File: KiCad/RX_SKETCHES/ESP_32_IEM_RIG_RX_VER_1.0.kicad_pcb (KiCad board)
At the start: 2 copper layers, 55.2 x 90.5 mm, 69 parts, among them J1 AudioJack3, J6 USB_C_Receptacle_USB2.0_16P, Q1 S8050, Q2 S8050, SW2 FILTER_MODE, SW3 SOFT_MUTE, SW4 ON/OFF, U1 PCM5102, U2 ESP32-WROOM-32U, U3 MAX97220AETE_T, U4 LM3940IMPX-3.3_NOPB, U5 CP2102C-Axx-xQFN24

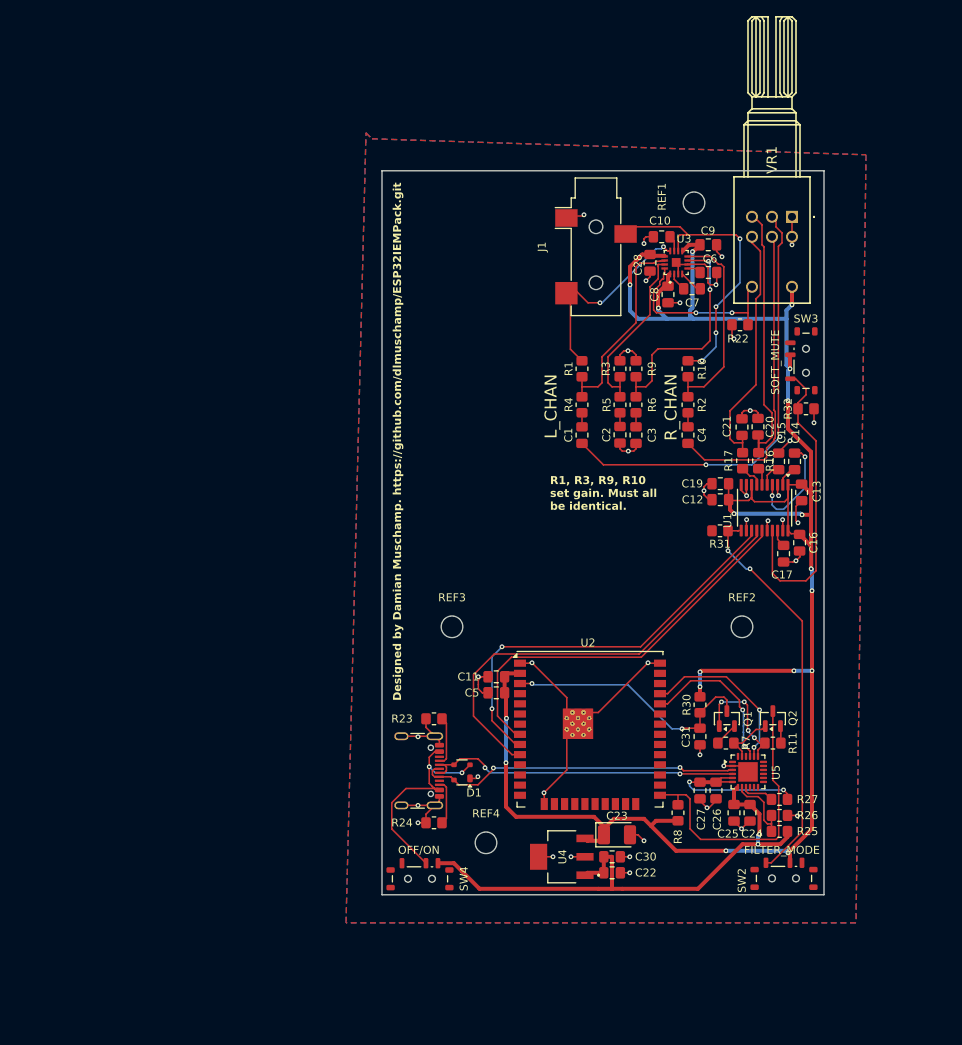
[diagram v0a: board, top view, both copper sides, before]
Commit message: Ship RX+TX v1 boards: routed PCBs, JLCPCB exports, README for order spin.
Freeze electrical intent for fab (Gerbers/BOM/CPL), document firmware design philosophy and summer timeline, and drop stale ERC/DRC/fab clutter.

Co-authored-by: Cursor <cursoragent@cursor.com>
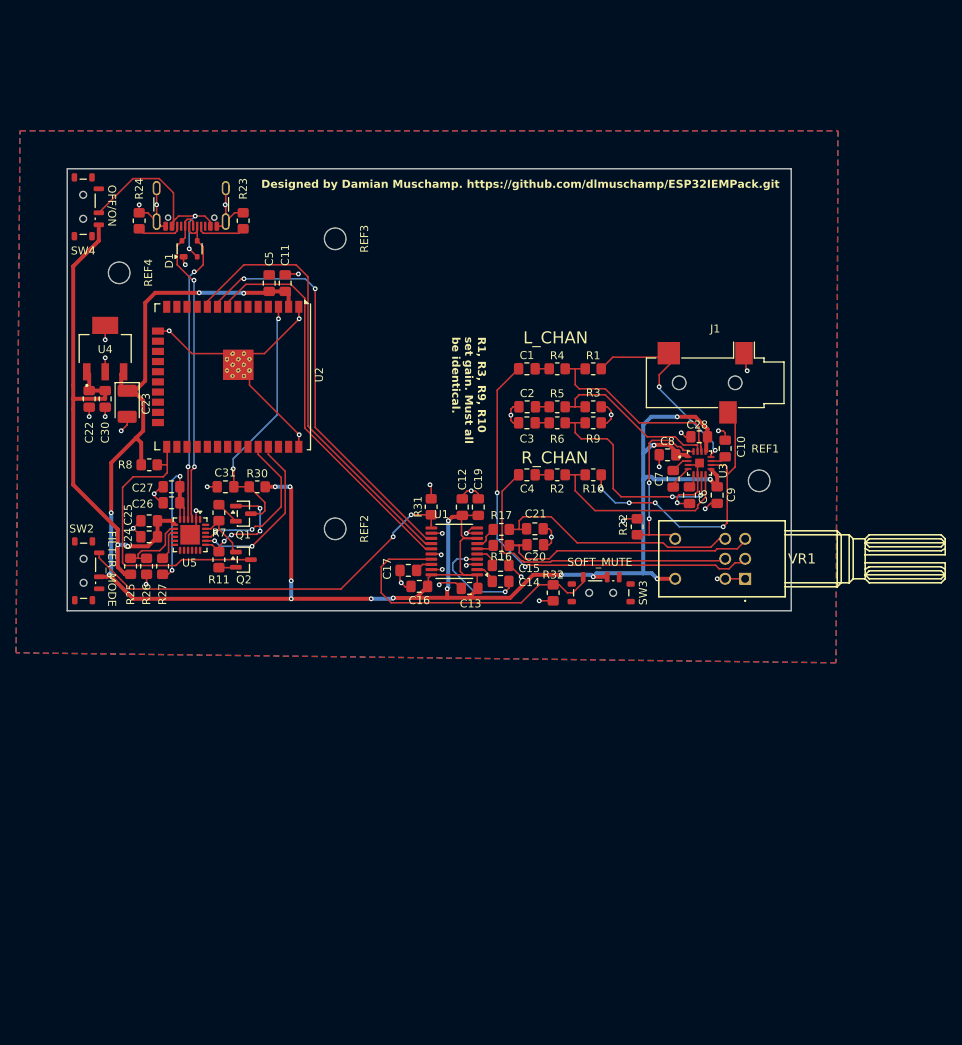
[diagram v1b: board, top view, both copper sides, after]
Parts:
- moved SW2 95.6 mm to (59.2, 88.5), turned to -90 degrees
- moved SW4 94.0 mm to (59.1, 43.0), turned to -90 degrees
- moved C22 88.2 mm to (59.9, 67.0), turned to -90 degrees
- moved R25 87.6 mm to (65.1, 87.9), turned to 90 degrees
- moved U4 85.4 mm to (61.9, 60.7), turned to 90 degrees
- moved C30 85.4 mm to (61.9, 67.0), turned to -90 degrees
- moved R26 85.0 mm to (67.1, 87.9), turned to -90 degrees
- moved REF4 84.7 mm to (63.6, 51.2), turned to -90 degrees
- moved R24 83.8 mm to (66.2, 44.8), turned to 90 degrees
- moved C24 82.6 mm to (67.4, 84.2), turned to 180 degrees
- moved R27 82.4 mm to (69.1, 87.9), turned to -90 degrees
- moved C25 81.7 mm to (67.4, 82.2), turned to 180 degrees
- moved C23 81.6 mm to (64.7, 67.6), turned to -90 degrees
- moved R8 79.1 mm to (67.4, 75.2), turned to 0 degrees
- moved C26 77.0 mm to (70.2, 80.0), turned to 180 degrees
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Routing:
- net GND: track 130.7 -> 130.3 mm, vias 39 -> 40
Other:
- board size 55.2 x 90.5 mm -> 90.5 x 55.2 mm

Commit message: Refresh TX/RX silk artwork and regenerate JLCPCB gerbers.
Cosmetic pass: silkscreen, QR codes, font, and screw hole moves — BOM/CPL unchanged.

Co-authored-by: Cursor <cursoragent@cursor.com>
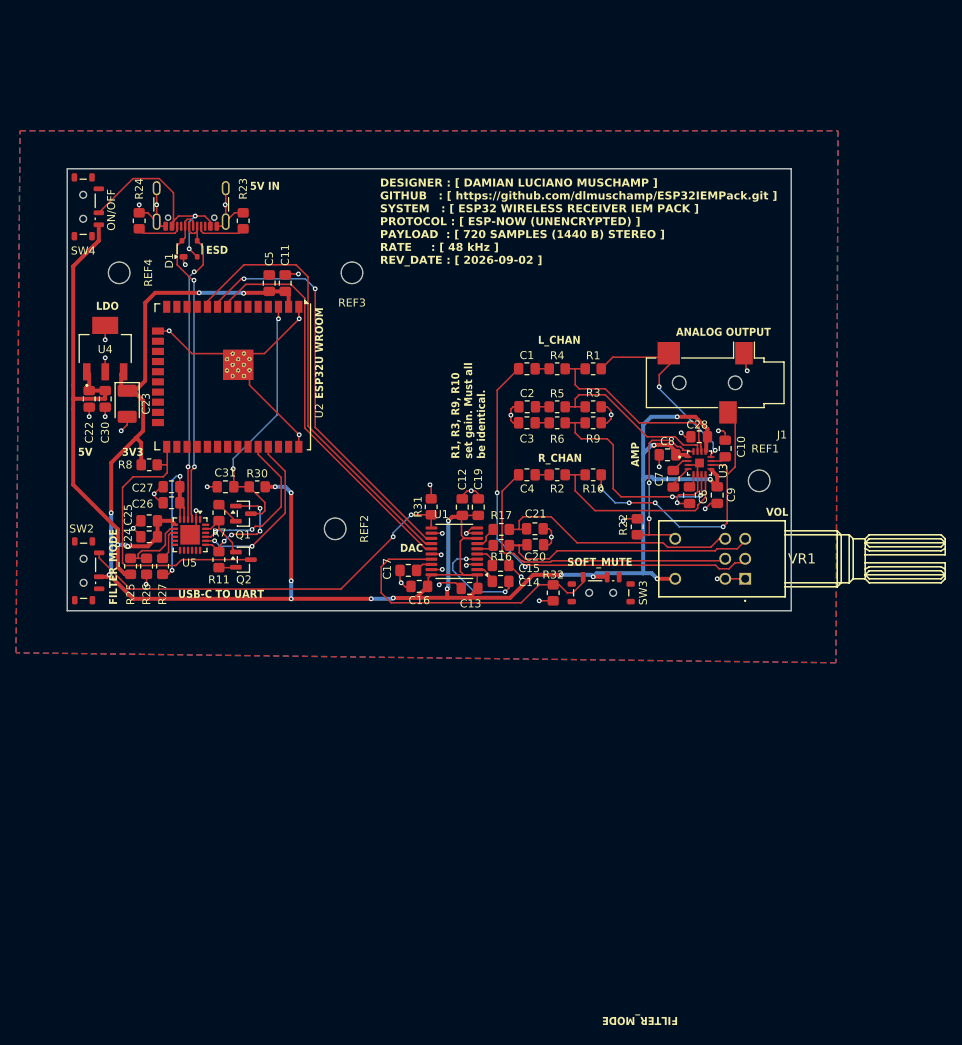
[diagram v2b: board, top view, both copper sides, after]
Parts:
- moved REF3 4.74 mm to (92.8, 51.2)
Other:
- board text added: "3V3"
- board text added: "5V"
- board text added: "5V IN"
- board text added: "AMP"
- board text added: "ANALOG OUTPUT"
- board text added: "DAC"
- board text added: "DESIGNER : [ DAMIAN LUCIANO MUSCHAMP ] GITHUB : [ https://github.com/dlmuschamp/ESP32IEMPack.git ] SYSTEM : [ ESP32 WIRELESS RECEIVER IEM PACK ]r PROTOCOL : [ ESP-NOW (UNENCRYPTED) ]r PAYLOAD : [ 720 SAMPLES (1440 B) STEREO ]r RATE : [ 48 kHz ] REV_DATE : [ 2026-09-02 ]"
- board text added: "ESD"
- board text added: "ESP32U WROOM"
- board text added: "LDO"
- board text added: "ON/OFF"
- board text added: "USB-C TO UART"
- board text added: "VOL"
- board text removed: "Designed by Damian Muschamp. https://github.com/dlmuschamp/ESP32IEMPack.git"
- board text removed: "OFF/ON"
